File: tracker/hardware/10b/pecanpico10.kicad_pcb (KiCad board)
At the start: 2 copper layers, 23 x 50 mm, 121 parts, among them IC1 SPV1040T, IC10 AS213-92LF, IC2 TPS62260DRVR, IC3 ADP322ACPZ-115-R7, IC4 Si4464-B1B-FM, IC5 STM32F413RHT6, IC6 EVA-7M or EVA-M8, IC7 PAC1720-1-AIA-TR, IC8 TPS62260DRVR, IC9 BME280, J1 DM3AT-SF-PEJM5, J2 CONN_01X15, P1 CONN_01X25, P3 ZX62-B-5PA(33), P4 SMA, Q1 FDN306P, X1 KT2016K26000BCW18ZAS

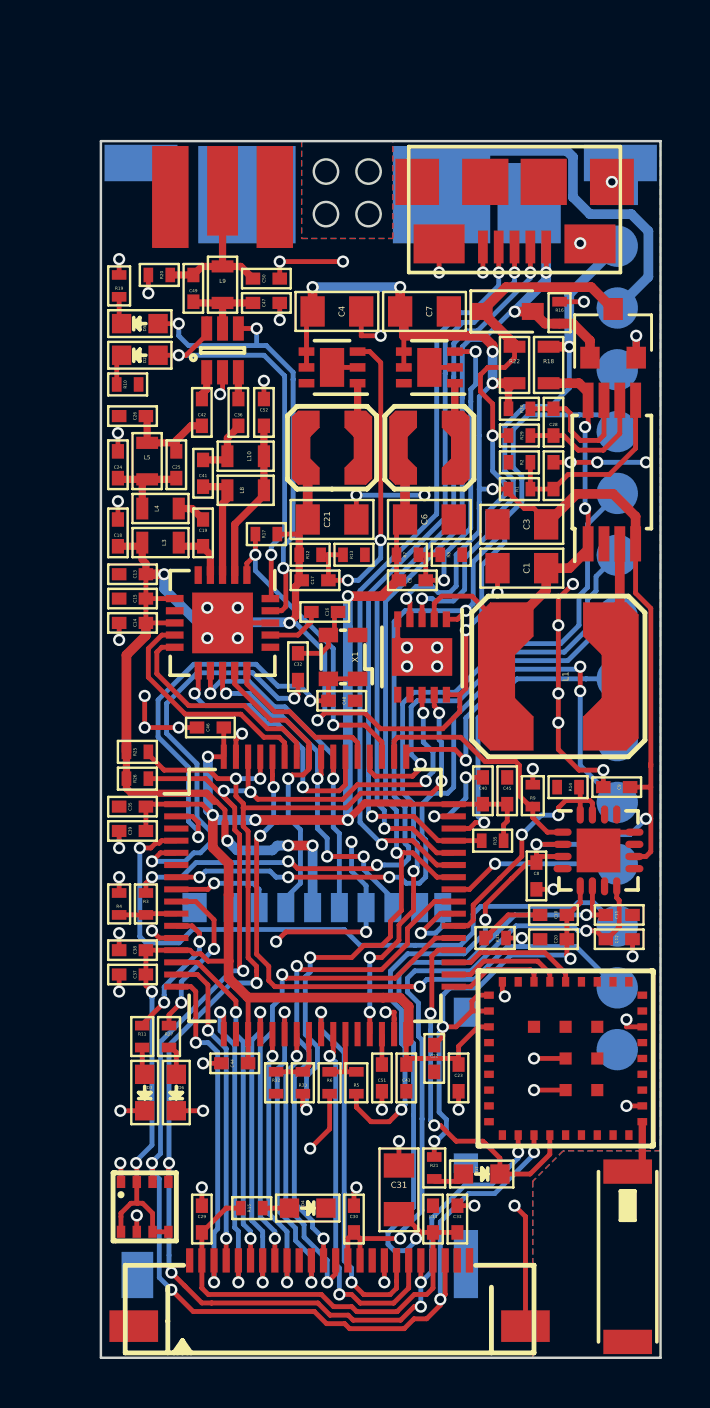
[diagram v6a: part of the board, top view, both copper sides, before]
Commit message: Added 2m bandpass trap filter in GPS rx Removed unnecessary resistor Edited/Added schematic comments
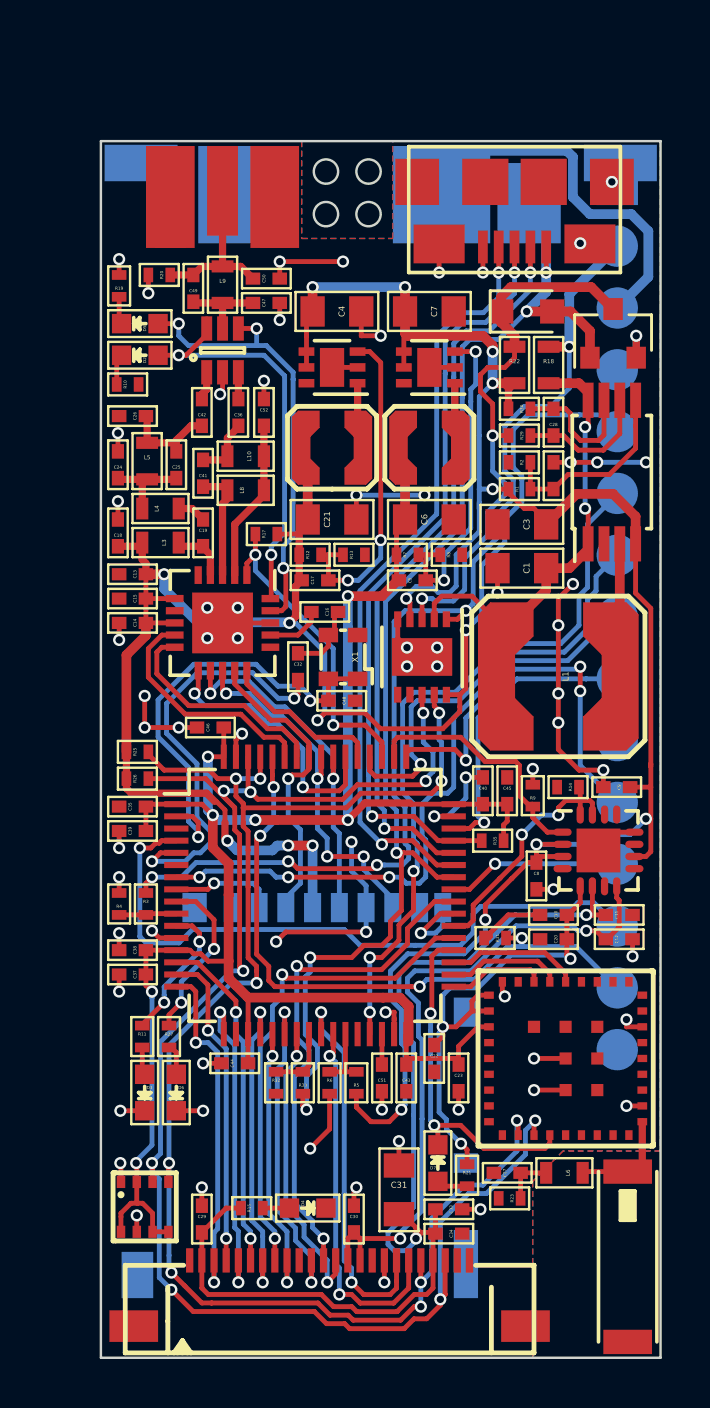
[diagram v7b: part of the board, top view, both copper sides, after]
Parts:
- removed R16: 10k, pecanpico:R_0402
- added C27: 1n, pecanpico:C_0402, F.Cu at (63.8, 117.0)
- added L6: 1.2nH, pecanpico:R_0603, F.Cu at (66.2, 117.0)
- added R23: 1M, pecanpico:R_0402, F.Cu at (63.9, 118.0)
- moved D7 1.86 mm to (61.0, 116.6), turned to 270 degrees
- moved R21 1.38 mm to (62.1, 117.1)
- moved C34 0.88 mm to (61.4, 119.5), turned to 180 degrees
- moved D1 0.80 mm to (64.6, 81.6)
- moved C33 0.53 mm to (61.4, 118.5), turned to 180 degrees
- moved C7 0.20 mm to (60.6, 81.6)
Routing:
- net GND: track 90.7 -> 84.6 mm, vias 72 -> 70
- net Net-(C27-Pad2): track 0.00 -> 2.10 mm
- net Net-(AE1-Pad1): track 2.47 -> 4.34 mm
- net /SENSE_BAT-: track 79.8 -> 80.9 mm
- net /I2C_SDA: track 65.0 -> 66.0 mm
- net /I2C_SCL: track 63.6 -> 64.6 mm
- net VDD: track 24.0 -> 23.0 mm
- net /GPS_TIMEPULSE: track 15.3 -> 14.6 mm

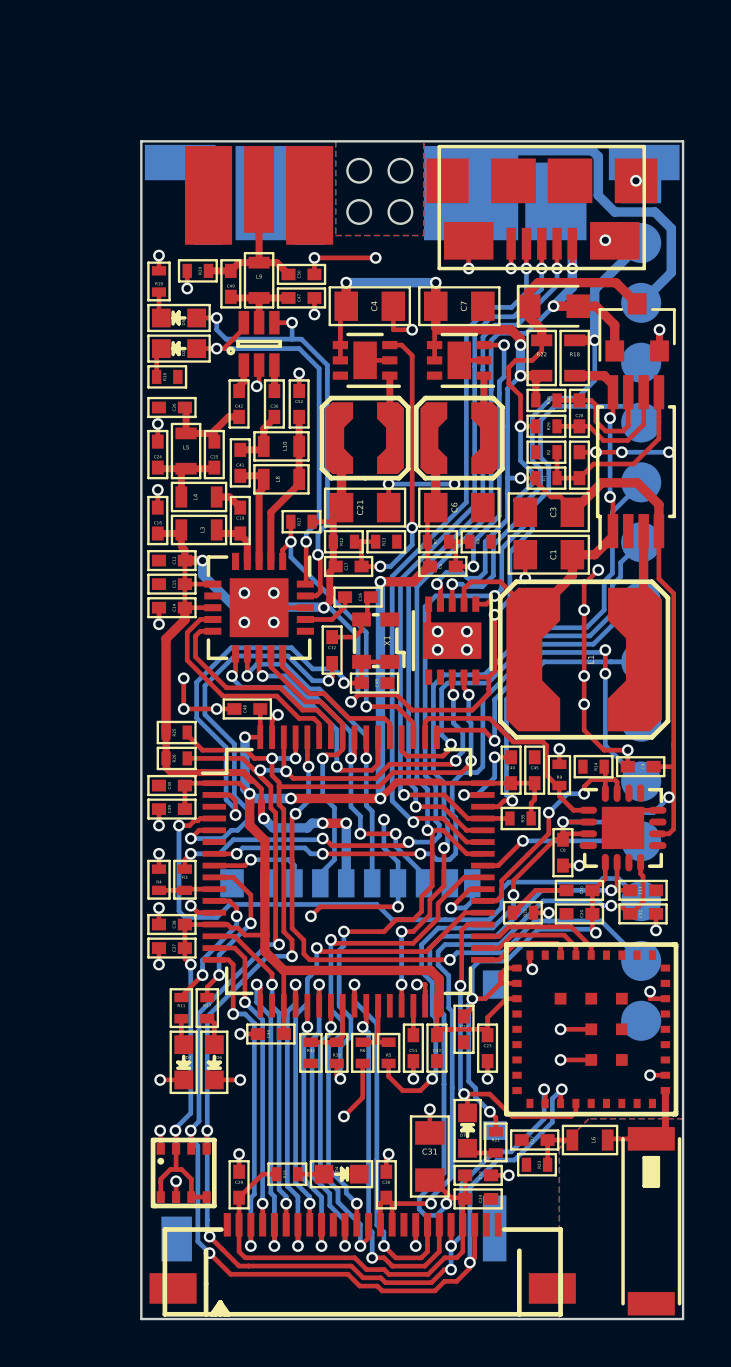
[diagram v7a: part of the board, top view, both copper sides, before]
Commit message: Added SAW Filter Optimized Antenna connections Created SAW Filter pad
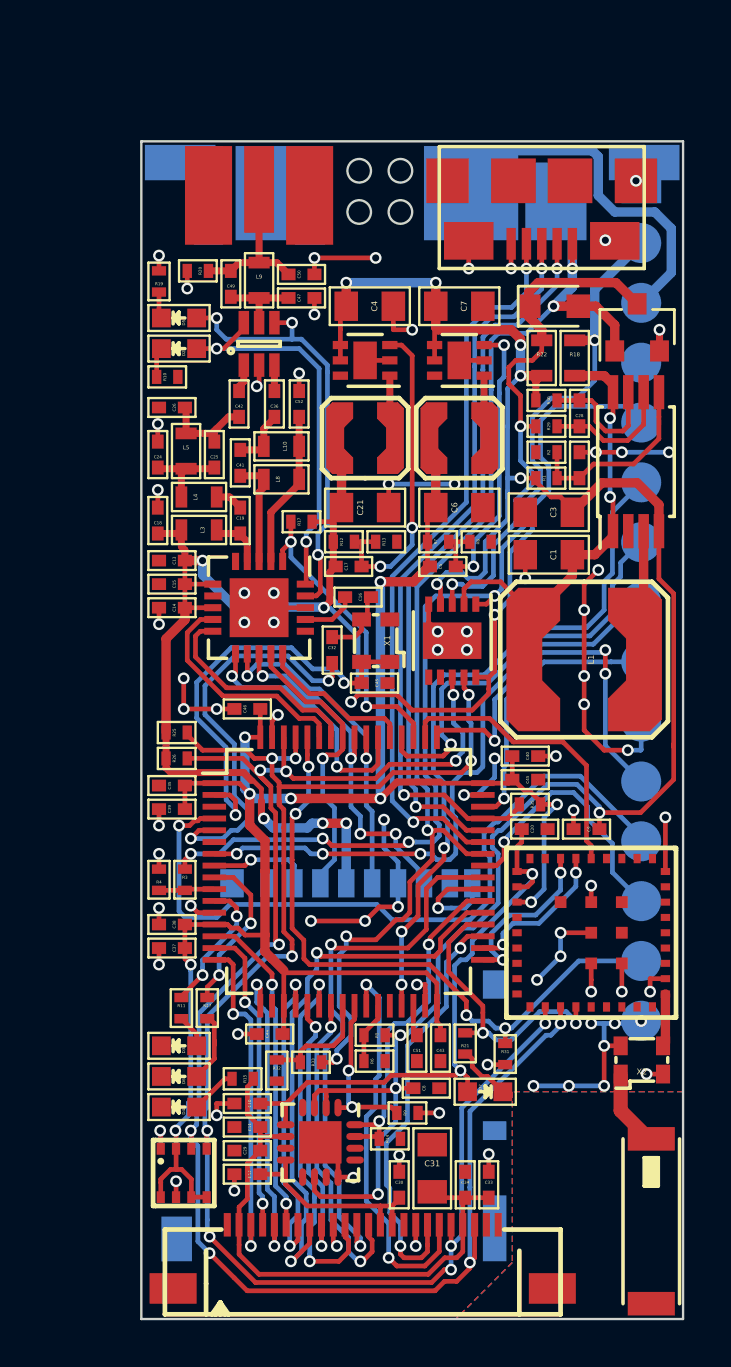
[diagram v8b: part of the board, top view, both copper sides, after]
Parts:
- removed C22, C23: 100n, pecanpico:C_0402
- removed C27: 1n, pecanpico:C_0402
- removed L6: 1.2nH, pecanpico:R_0603
- removed R23: 1M, pecanpico:R_0402
- added X2: SF2316H, pecanpico:tcxo, F.Cu at (68.3, 113.6)
- moved C12 20.1 mm to (51.6, 118.5), turned to 180 degrees
- moved C11 19.6 mm to (51.6, 116.5), turned to 180 degrees
- moved IC3 18.5 mm to (54.7, 117.1), turned to 270 degrees
- moved R14 18.0 mm to (57.6, 117.0), turned to 0 degrees
- moved C10 16.8 mm to (51.6, 115.5)
- moved R9 15.7 mm to (58.4, 115.8), turned to 0 degrees
- moved C8 11.6 mm to (59.2, 114.8), turned to 0 degrees
- moved D4 7.47 mm to (48.7, 115.6), turned to 0 degrees
- moved R31 6.05 mm to (62.5, 113.3), turned to 270 degrees
- moved R15 4.47 mm to (51.4, 114.4), turned to 180 degrees
- moved R21 4.40 mm to (60.9, 112.9), turned to 90 degrees
- moved IC6 4.10 mm to (66.2, 108.2)
- moved C20 4.07 mm to (63.8, 103.8), turned to 0 degrees
- moved C9 3.51 mm to (66.0, 103.8)
- moved D7 1.81 mm to (61.7, 115.0), turned to 180 degrees
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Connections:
- D7 pad 1: /GPS_TIMEPULSE -> Net-(D7-Pad1)
- D7 pad 2: Net-(D7-Pad2) -> /VCC_GPS
- IC5 pad 25: /CAM_VSYNC -> /GPS_EN
- IC5 pad 35: /GPS_RESET -> /CAM_VSYNC
- IC5 pad 50: /GPS_EN -> /GPS_RESET
- IC6 pad 1: Net-(AE1-Pad1) -> Net-(IC6-Pad1)
- J2 pad 12: /IO_PA8 -> /IO_PC15
- J2 pad 13: /IO_PC15 -> /IO_PA8
- P1 pad 25: GND -> Net-(P1-Pad25)
- R21 pad 1: /VCC_GPS -> Net-(D7-Pad1)
- R21 pad 2: Net-(D7-Pad2) -> /GPS_TIMEPULSE
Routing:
- net VDDA: track 44.4 -> 24.9 mm, vias 2 -> 0
- net +1V8: track 27.2 -> 9.13 mm, vias 2 -> 0
- net GND: track 84.6 -> 93.6 mm, vias 70 -> 80
- net /SENSE_BAT-: track 80.9 -> 89.8 mm
- net /GPS_RESET: track 5.47 -> 12.4 mm
- net /IO_PC15: track 27.1 -> 31.4 mm
- net /IO_PA8: track 7.16 -> 11.4 mm
- net /CAM_EN: track 10.6 -> 14.8 mm
- net /CAM_PCLK: track 20.2 -> 24.2 mm
- net /VCC_GPS: track 21.4 -> 25.0 mm, vias 3 -> 2
- net /GPS_RXD: track 4.00 -> 7.28 mm, vias 0 -> 2
- net /GPS_EN: track 10.3 -> 7.08 mm, vias 0 -> 2
- net /CAM_D8: track 13.6 -> 16.4 mm
- net /CAM_XCLK: track 21.1 -> 23.7 mm
- net /I2C_SCL: track 64.6 -> 67.1 mm
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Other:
- net class Default: trace_width 0.4 -> 0.2
- board text added: "May 2018"
- board text added: "PA8/ SCL"
- board text added: "PC15/SDA"
- board text removed: "Apr 2018"
- board text removed: "PA8/SCL"
- board text removed: "PC15/ SDA"
